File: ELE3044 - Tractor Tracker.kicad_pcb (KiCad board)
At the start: 4 copper layers, 100 x 100 mm, 62 parts, among them J1 Power Terminals, J2 USB_B_Micro, J3 Screw_Terminal_01x12, J4 SMA-Female, K1 EC2-3TNU, K2 EC2-3TNU, Q1 Q_PMOS_DGS, Q2 NX3008, Q3 NX3008, Q4 NX3008, Q5 NX3008, Q6 NPN, Q7 NPN, SW1 SW_Push, SW2 SW_Push, U1 NCP1117-3.3_SOT223, U2 CY7C64225, U3 MAX-M8Q, U4 ESP32-S2-WROVER

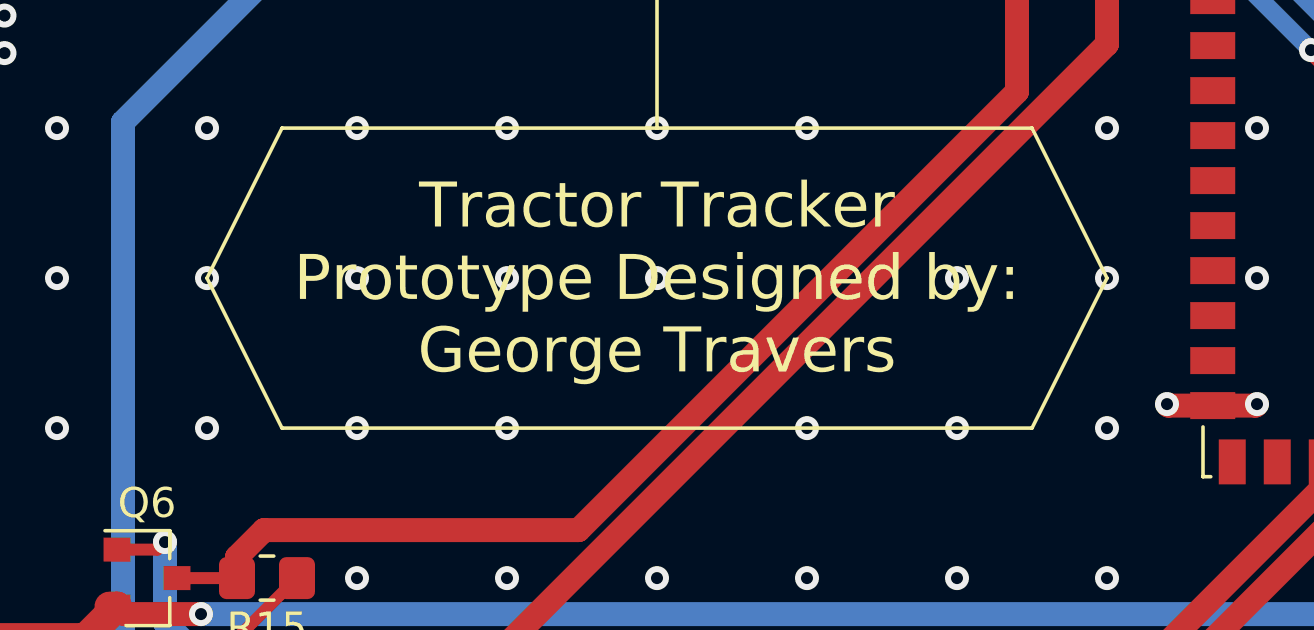
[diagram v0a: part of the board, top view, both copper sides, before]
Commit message: Added new output files, a render image and PDF schematic
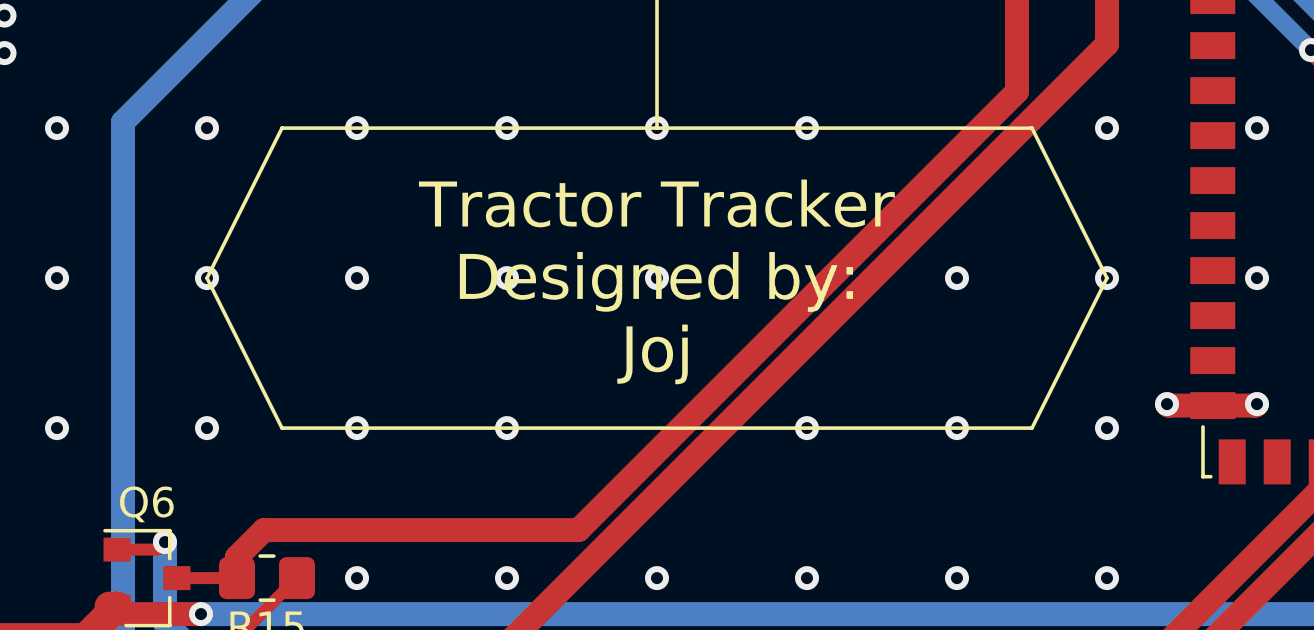
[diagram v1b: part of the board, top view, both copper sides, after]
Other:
- board text added: "Tractor Tracker Designed by: Joj"
- board text removed: "Tractor Tracker Prototype Designed by: George Travers"
